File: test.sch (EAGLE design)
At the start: 15 parts, among them U1_1 2.1MMJACKTHM, U1_5 TMP36

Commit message: makefile fixes'
git-svn-id: svn+ssh://bbfs-01.calit2.net/grw/Gordon/svn/trunk/Gadgets/Tools/CircuitsByCode@19963 2cf53259-273a-af40-bda6-69d31023b8ec
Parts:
- removed C1_5: 0.1uF, Capacitors:CAPACITOR-0805-0.1UF-10%-25V
- removed LED1, LED1_4: RGBLED_CA-5MM, Components:RGBLED_CA-5MM
- removed LED1_0: (no value), Components:LED10MM
- removed R1_0: (no value), resistor:R-US_0204/5
- removed R1_4, R2_4: 90, Components:RESISTOR-TH-1/6W
- removed R3_4: 160, Components:RESISTOR-TH-1/6W
- removed U$2_2: ARDUINO_MICRO_REV03J-BOB, BOBs:ARDUINO_MICRO_REV03J-BOB
- removed U1_1: 2.1MMJACKTHM, Components:2.1MMJACKTHM
- removed U1_5: TMP36, Components:TEMP-SENSOR-TMP36-SPARKFUN10988-TH
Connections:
- removed net +3V3_2: U$2_2.3V3
- removed net A0_2: U$2_2.A0
- removed net A1_2: U$2_2.A1
- removed net A2_2: U$2_2.A2
- removed net A3_2: U$2_2.A3
- removed net A4_2: U$2_2.A4
- removed net A5_2: U$2_2.A5
- removed net D0: LED1_0.A, U$2_2.D0/RX
- removed net D10: R2_4.2, U$2_2.IO10*
- removed net D11: R1_4.2, U$2_2.IO11*
- removed net D12_2: U$2_2.IO12*
- removed net D13_2: U$2_2.IO13*
- removed net D1_2: U$2_2.D1/TX
- removed net D2_2: U$2_2.D2/SDA
- removed net D3_2: U$2_2.D3/SCL
- removed net D7_2: U$2_2.D7
- removed net D8_2: U$2_2.IO8
- removed net D9: R3_4.2, U$2_2.IO9*
- removed net GND: C1_5.2, R1_0.1, U$2_2.GND, U$2_2.GND1, U1_1.RING
- removed net MISO_2: U$2_2.MISO
- removed net MOSI_2: U$2_2.MOSI
- removed net N$1_0: LED1_0.C, R1_0.2
- removed net N$1_4: LED1_4.BLUE, R1_4.1
- removed net N$2_4: LED1_4.GREEN, R2_4.1
- removed net N$3_4: LED1_4.RED, R3_4.1
- removed net RING_SW_1: U1_1.RING_SW
- removed net SCK_2: U$2_2.SCK
- removed net VIN_2: U$2_2.VIN
- net D4: no longer U$2_2.D4*
- net D5: no longer U$2_2.D5*
- net D6: no longer U$2_2.D6*
- net TIP: no longer C1_5.1, LED1_4.VCC, U$2_2.+5V, U1_1.TIP

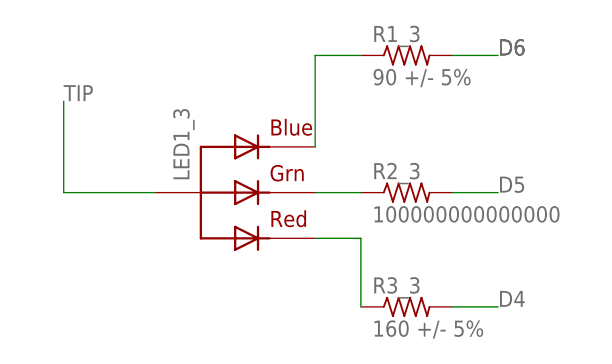
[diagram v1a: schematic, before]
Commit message: Cleaner error reporting.
Improved sanity checks.

Support for Device field in part databases

Removed terrible bug that was causing exponential slowdown over time by doubling the number of wires in the file every time it was loaded.  
Dramatic improvements in performance!

Fixed arduino schematic to only use GENERIC Components for things we can actually resolve.

Updated Base.lbr to support our new device model.





git-svn-id: svn+ssh://bbfs-01.calit2.net/grw/Gordon/svn/trunk/Gadgets/Tools/CircuitsByCode@20209 2cf53259-273a-af40-bda6-69d31023b8ec
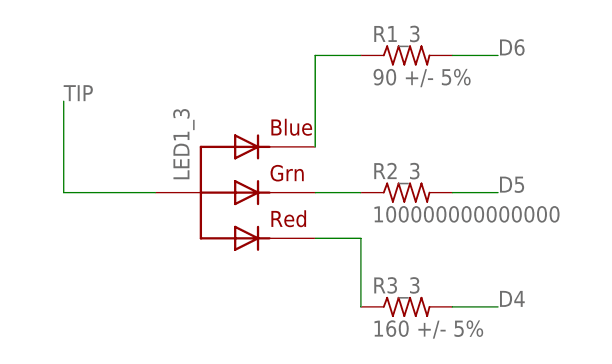
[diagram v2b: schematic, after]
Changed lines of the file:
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@@
 <wire x1="86.36" y1="76.2" x2="91.44" y2="76.2" width="0.1524" layer="91"/>
-<label x="91.44" y="76.2" size="1.778" layer="95"/>
 <label x="91.44" y="76.2" size="1.778" layer="95"/>
 </segment>
